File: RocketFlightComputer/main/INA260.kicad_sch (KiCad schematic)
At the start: 2 parts

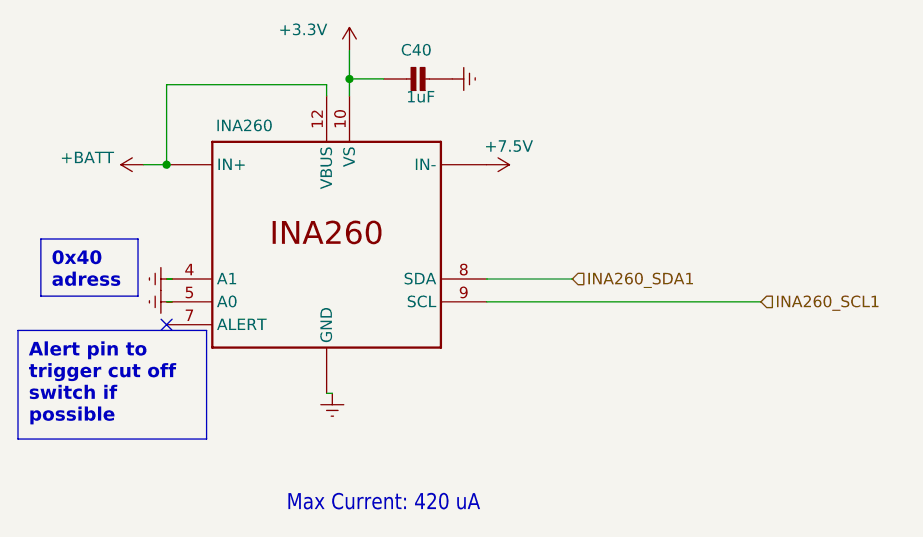
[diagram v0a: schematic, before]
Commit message: First pass of verification and validation of pcb design
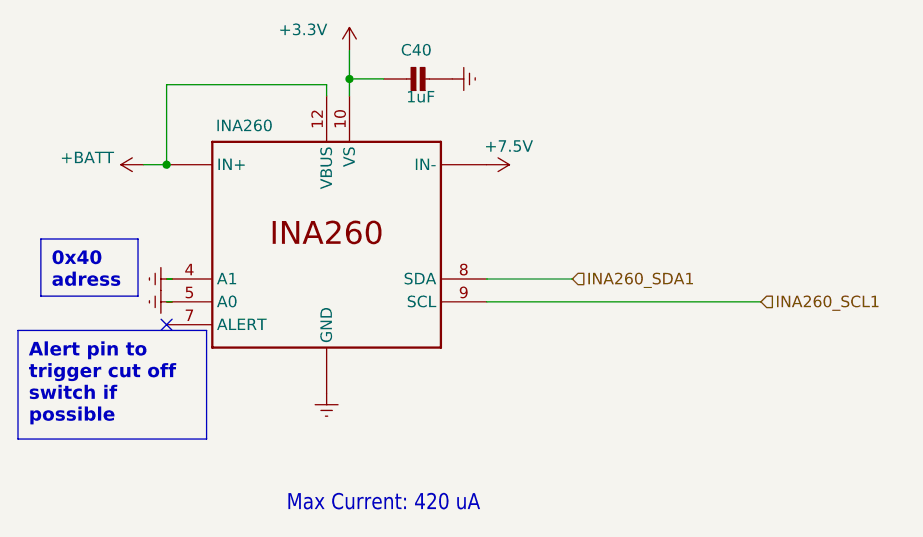
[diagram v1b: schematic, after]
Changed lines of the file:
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@@
-	(wire
-		(pts
-			(xy 95.25 88.9) (xy 95.885 88.9)
-		)
-		(stroke
-			(width 0)
-			(type default)
-		)
-	)
 	(wire
 		(pts
@@
 	(symbol
 		(lib_id "power:GNDREF")
-		(at 95.885 88.9 0)
+		(at 95.25 88.9 0)
 		(mirror y)
 		(unit 1)
@@
 		(fields_autoplaced yes)
 		(property "Reference" "#PWR0109"
-			(at 95.885 95.25 0)
+			(at 95.25 95.25 0)
 			(effects
 				(font
@@
 		)
 		(property "Value" "GNDREF"
-			(at 96.52 92.71 90)
+			(at 95.885 92.71 90)
 			(effects
 				(font
@@
 		)
 		(property "Footprint" ""
-			(at 95.885 88.9 0)
+			(at 95.25 88.9 0)
 			(effects
 				(font
@@
 		)
 		(property "Datasheet" ""
-			(at 95.885 88.9 0)
+			(at 95.25 88.9 0)
 			(effects
 				(font
@@
 		)
 		(property "Description" ""
-			(at 95.885 88.9 0)
-			(effects
-				(font
+			(at 95.25 88.9 0)
+			(effects
+				(font

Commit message: Addition of all components in BOM, metal mounting plates, need to check psram if its ok for signals to pass under, all components need a double check
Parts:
- C40: LCSC (none) -> C1592
- INA1: renamed from INA260; LCSC (none) -> C2155885; Mouser Part Number (none) -> 595-INA260AIPWR
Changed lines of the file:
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@@
 		(dnp no)
 		(fields_autoplaced yes)
-		(property "Reference" "#PWR0111"
+		(property "Reference" "#PWR0117"
 			(at 115.57 53.975 0)
 			(effects
@@
 			(project "main"
 				(path "/27195d1d-92b2-40df-ada5-3b20841577e7/125f95e9-6bcc-4b33-8d0b-519410cf48bf"
-					(reference "#PWR0111")
+					(reference "#PWR0117")
 					(unit 1)
 				)
@@
 		(dnp no)
 		(fields_autoplaced yes)
-		(property "Reference" "#PWR0108"
+		(property "Reference" "#PWR0114"
 			(at 71.755 78.74 0)
 			(effects
@@
 			(project "main"
 				(path "/27195d1d-92b2-40df-ada5-3b20841577e7/125f95e9-6bcc-4b33-8d0b-519410cf48bf"
-					(reference "#PWR0108")
+					(reference "#PWR0114")
 					(unit 1)
 				)
@@
 		(dnp no)
 		(fields_autoplaced yes)
-		(property "Reference" "#PWR0109"
+		(property "Reference" "#PWR0115"
 			(at 95.25 95.25 0)
 			(effects
@@
 			(project "main"
 				(path "/27195d1d-92b2-40df-ada5-3b20841577e7/125f95e9-6bcc-4b33-8d0b-519410cf48bf"
-					(reference "#PWR0109")
+					(reference "#PWR0115")
 					(unit 1)
 				)
@@
 		(on_board yes)
 		(dnp no)
-		(property "Reference" "#PWR0114"
+		(property "Reference" "#PWR0118"
 			(at 109.22 63.5 0)
 			(effects
@@
 			(project "main"
 				(path "/27195d1d-92b2-40df-ada5-3b20841577e7/125f95e9-6bcc-4b33-8d0b-519410cf48bf"
-					(reference "#PWR0114")
+					(reference "#PWR0118")
 					(unit 1)
 				)
@@
 		(dnp no)
 		(fields_autoplaced yes)
-		(property "Reference" "#PWR0107"
+		(property "Reference" "#PWR0113"
 			(at 71.755 76.2 0)
 			(effects
@@
 			(project "main"
 				(path "/27195d1d-92b2-40df-ada5-3b20841577e7/125f95e9-6bcc-4b33-8d0b-519410cf48bf"
-					(reference "#PWR0107")
+					(reference "#PWR0113")
 					(unit 1)
 				)
@@
 		(on_board yes)
 		(dnp no)
-		(property "Reference" "#PWR0154"
+		(property "Reference" "#PWR0112"
 			(at 78.74 63.5 0)
 			(effects
@@
 			(project "main"
 				(path "/27195d1d-92b2-40df-ada5-3b20841577e7/125f95e9-6bcc-4b33-8d0b-519410cf48bf"
-					(reference "#PWR0154")
+					(reference "#PWR0112")
 					(unit 1)
 				)
@@
 		(on_board yes)
 		(dnp no)
-		(property "Reference" "#PWR0110"
+		(property "Reference" "#PWR0116"
 			(at 97.79 54.61 0)
 			(effects
@@
 			(project "main"
 				(path "/27195d1d-92b2-40df-ada5-3b20841577e7/125f95e9-6bcc-4b33-8d0b-519410cf48bf"
-					(reference "#PWR0110")
+					(reference "#PWR0116")
 					(unit 1)
 				)
@@
 		(on_board yes)
 		(dnp no)
-		(property "Reference" "INA260"
+		(property "Reference" "INA1"
 			(at 52.959 67.818 0)
 			(effects
@@
 			)
 		)
+		(property "LCSC" "C2155885 "
+			(at 95.25 71.12 0)
+			(effects
+				(font
+					(size 1.27 1.27)
+				)
+				(hide yes)
+			)
+		)
+		(property "Mouser Part Number" "595-INA260AIPWR"
+			(at 95.25 71.12 0)
+			(effects
+				(font
+					(size 1.27 1.27)
+				)
+				(hide yes)
+			)
+		)
 		(pin "1"
 		)
@@
 			(project "main"
 				(path "/27195d1d-92b2-40df-ada5-3b20841577e7/125f95e9-6bcc-4b33-8d0b-519410cf48bf"
-					(reference "INA260")
+					(reference "INA1")
 					(unit 1)
 				)
@@
 			(at 106.68 53.975 0)
 			(effects
+				(font
+					(size 1.27 1.27)
+				)
+				(hide yes)
+			)
+		)
+		(property "LCSC" "C1592 "
+			(at 106.68 53.975 0)
+			(effects

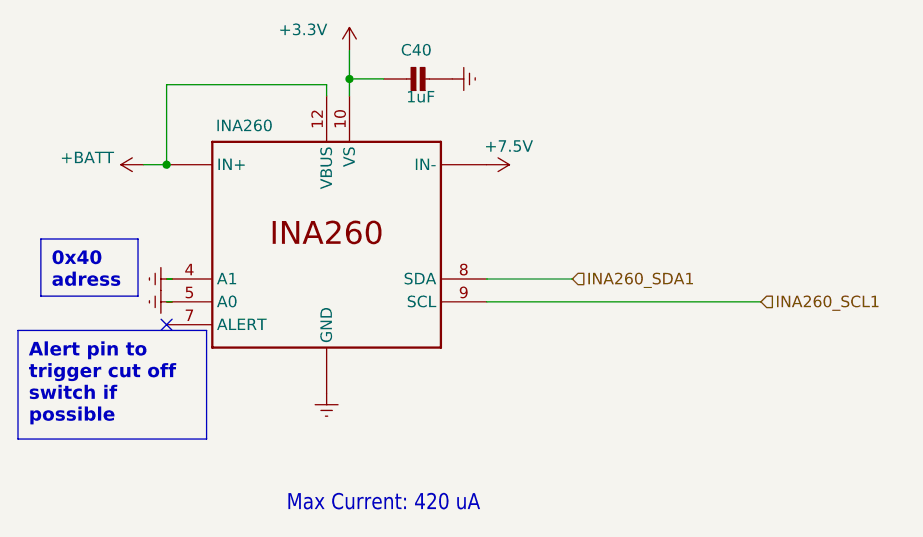
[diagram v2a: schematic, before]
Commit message: First commit with 0.1mm traces and 02mm by 0.43mm vias to fit pcbway standard manufacturing + corrections of PR'S like uart RX of component to TX of mcu
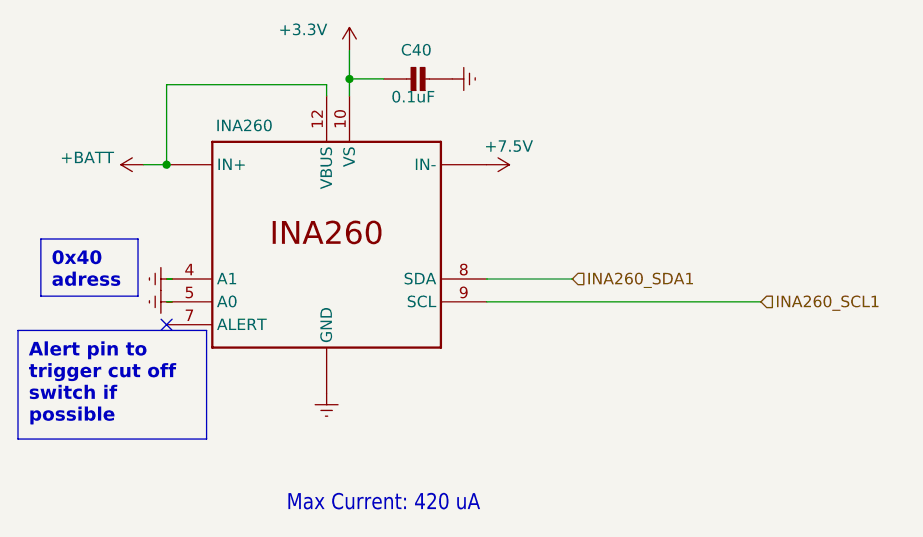
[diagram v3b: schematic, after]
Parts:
- C40: value 1uF -> 0.1uF; LCSC C1592 -> (none)
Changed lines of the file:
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@@
 			)
 		)
-		(property "Value" "1uF"
+		(property "Value" "0.1uF"
 			(at 107.315 55.245 90)
 			(effects
@@
 			)
 		)
-		(property "LCSC" "C1592 "
+		(property "LCSC" ""
 			(at 106.68 53.975 0)
 			(effects

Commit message: Change of winbond flash to other one supported by teensy bootloader since winbond is out of stock
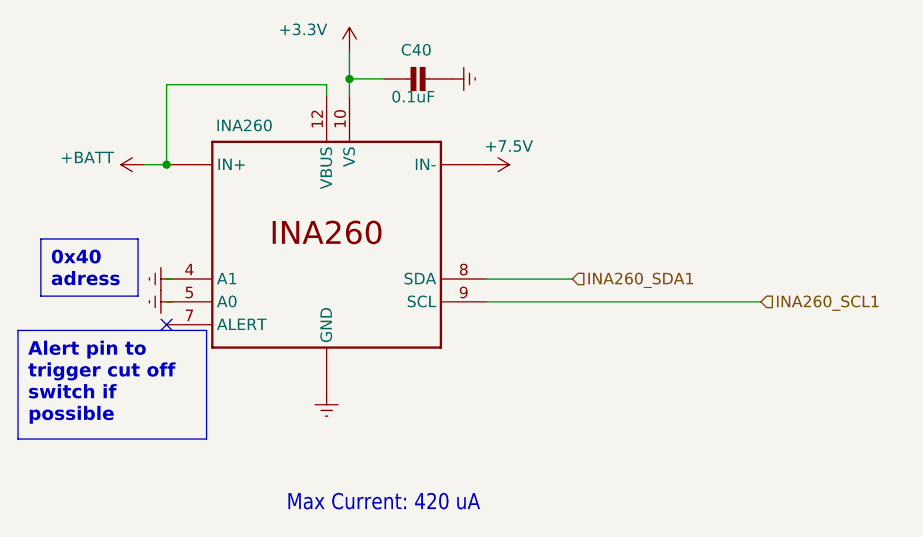
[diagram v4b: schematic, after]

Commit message: Corrected a few subsystems
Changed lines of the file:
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@@
 	(text_box "0x40 adress"
 		(exclude_from_sim no)
-		(at 63.5 71.755 0)
+		(at 92.075 72.39 0)
 		(size 10.795 6.35)
 		(margins 1.125 1.125 1.125 1.125)
 		(stroke
-			(width 0)
-			(type default)
-		)
-		(fill
-			(type none)
-		)
-		(effects
-			(font
-				(size 1.5 1.5)
-				(thickness 0.254)
-				(bold yes)
-			)
-			(justify left top)
-		)
-	)
-	(text_box "Alert pin to trigger cut off switch if possible"
-		(exclude_from_sim no)
-		(at 60.96 81.915 0)
-		(size 20.955 12.065)
-		(margins 1.125 1.125 1.125 1.125)
-		(stroke

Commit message: Corrections of mistake, revision of schematic is done and BOM revised, revision of pcb layout to do
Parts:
- C40: LCSC (none) -> C1590
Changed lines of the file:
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@@
 			)
 		)
-		(property "LCSC" ""
+		(property "LCSC" "C1590"
 			(at 106.68 53.975 0)
 			(hide yes)
